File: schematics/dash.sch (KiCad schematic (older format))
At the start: 28 parts, among them J1 BATT_CONN, J2 EXTERNAL_TRIGGER, J3 USB_OTG, SW1 SW_Push, SW2 SW_Push, U1 ESP-12E, U2 ch340g, U3 MCP73833, U4 HT7333, Y1 12Mhz

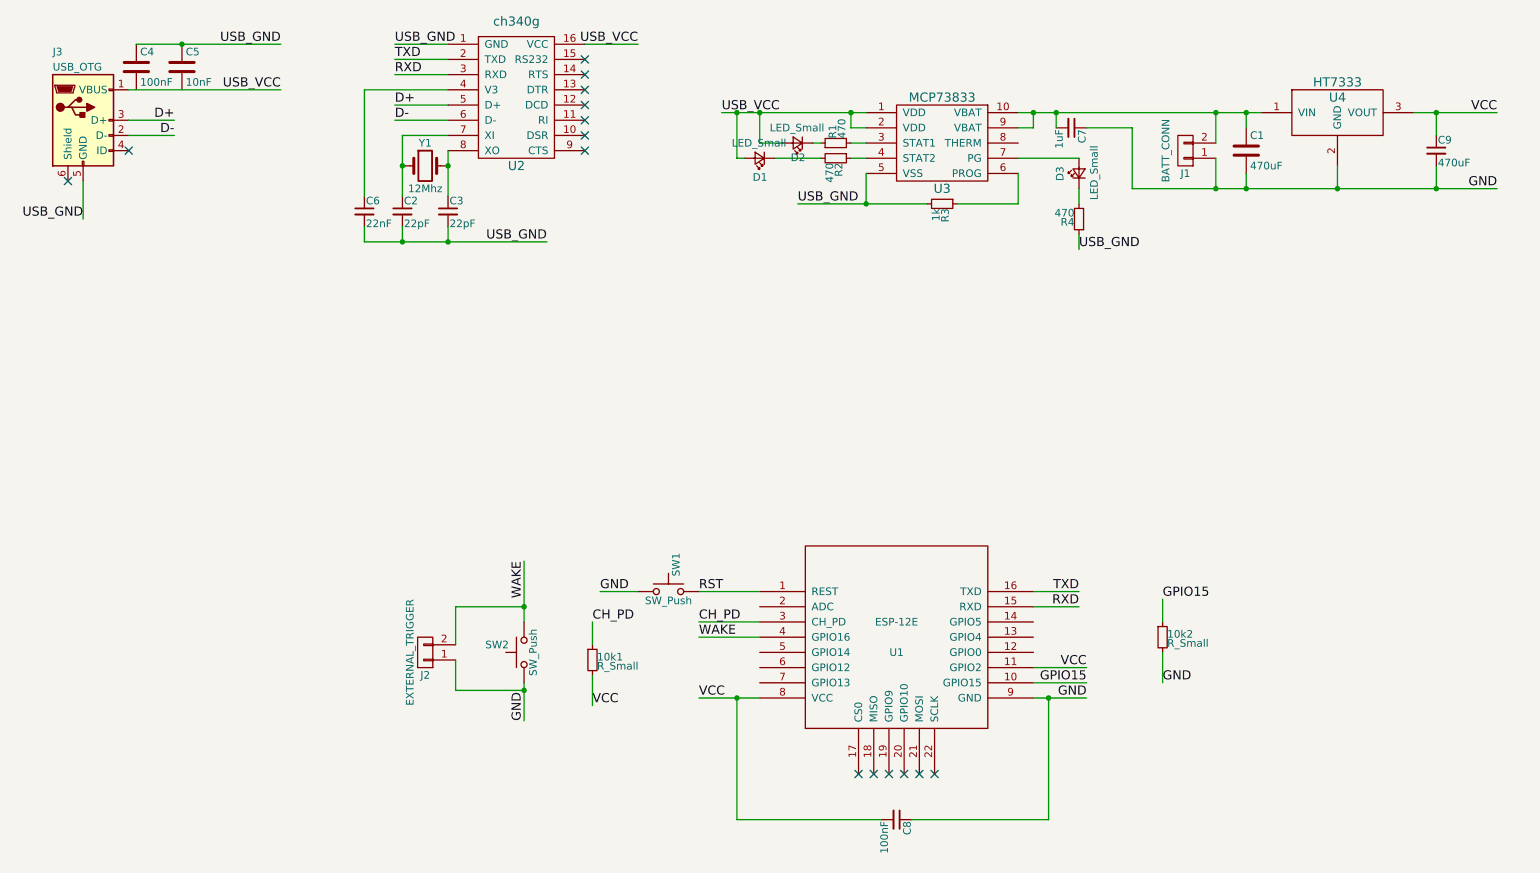
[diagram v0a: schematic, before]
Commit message: [add] Correction on boot mode pins
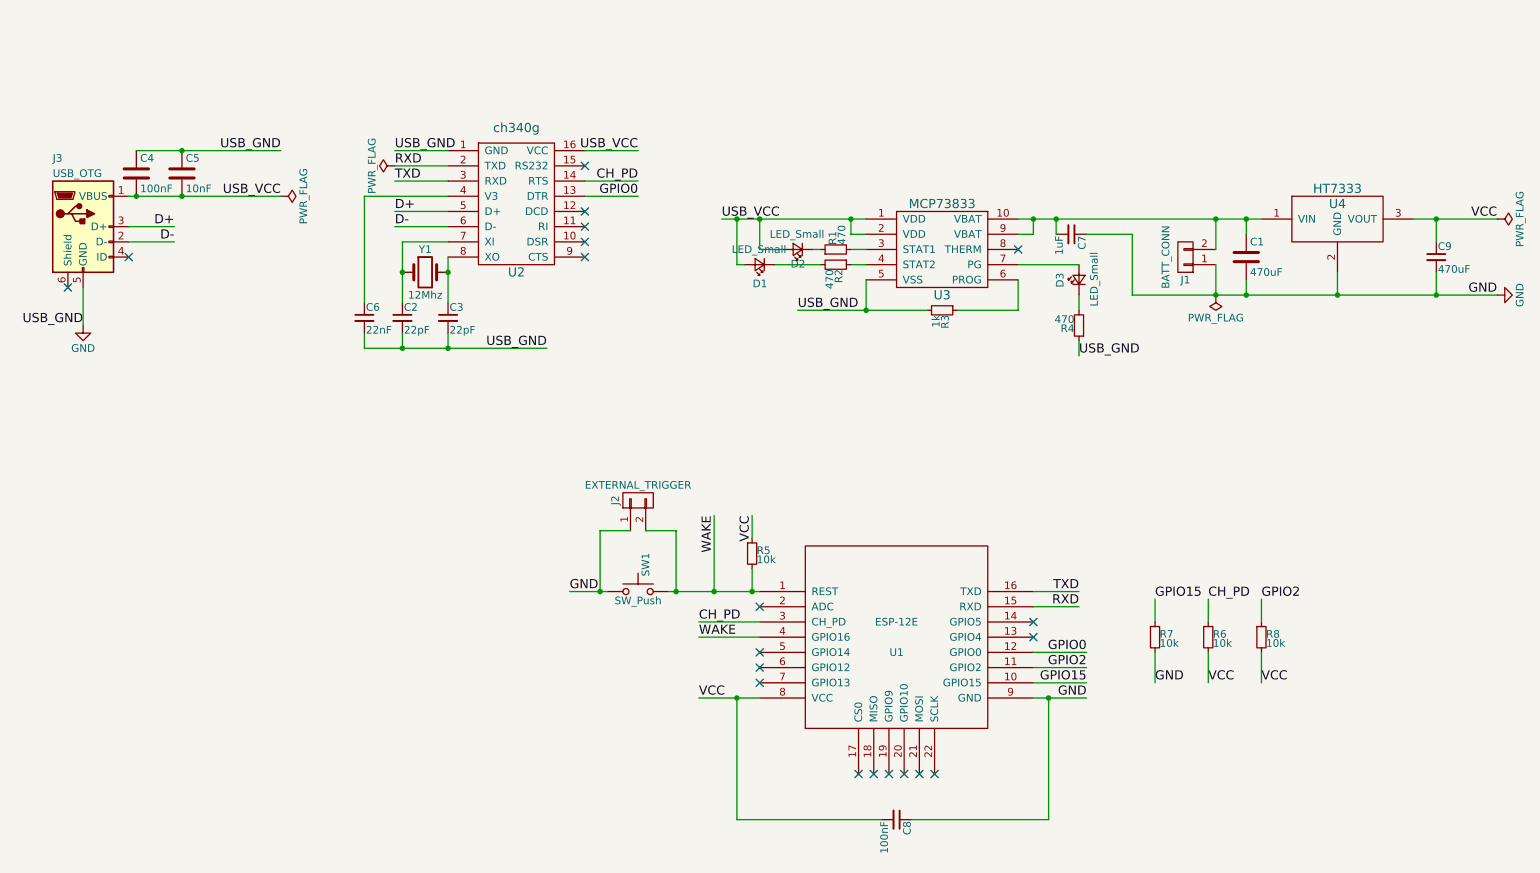
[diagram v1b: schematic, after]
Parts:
- removed 10k1, 10k2: R_Small, symbol R_Small
- removed SW2: SW_Push, symbol SW_Push
- added R5, R6, R7, R8: 10k, symbol R_Small
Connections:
- net RST is gone; now on net WAKE: SW1.2, U1.1 (REST)
- net USB_GND is gone; now on net GND: C2.2, C3.2, C4.1, C5.1, C6.2, J3.5 (GND), R3.2, R4.1, U2.1 (GND), U3.5 (VSS)
- net CH_PD: now also U2.14 (RTS), R6.1
- net GND: now also R7.2
- net GPIO15: now also R7.1
- net RXD: now also U2.2 (TXD); no longer U2.3 (RXD)
- net TXD: now also U2.3 (RXD); no longer U2.2 (TXD)
- net USB_VCC: now also C4.2, C5.2
- net VCC: now also R5.1, R6.2, R8.2; no longer U1.11 (GPIO2)
- net WAKE: now also R5.2
- net GPIO0: now reaches U1.12 (GPIO0)
- net GPIO0: now also U2.13 (DTR)
- new net GPIO2: R8.1, U1.11 (GPIO2)
- no-connect marks 15 -> 20
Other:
- moved on the sheet: C1, C2, C3, C4, C5, C6, C7, C9, D1, D2, D3, J1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

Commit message: add libraries to project and link symbols with footprints
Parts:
- C1, C2, C3, C4, C5, C6, C8: footprint (none) -> Capacitors_SMD:C_1206_HandSoldering
- C7: footprint (none) -> Capacitors_Tantalum_SMD:Tantalum_Case-A_EIA-3216-18_Hand
- C9: footprint (none) -> Capacitors_Tantalum_SMD:Tantalum_Case-D_EIA-7343-31_Hand
- D1, D2, D3: footprint (none) -> LEDs:LED_1206
- J1: footprint (none) -> Pin_Headers:Pin_Header_Angled_1x02
- J2: footprint (none) -> Pin_Headers:Pin_Header_Straight_1x02
- J3: footprint (none) -> Connect:USB_Micro-B; symbol USB_OTG -> USB_OTG-RESCUE-dash
- R1, R2, R3, R4, R5, R6, R7, R8: footprint (none) -> Resistors_SMD:R_1206_HandSoldering
- SW1: footprint (none) -> Buttons_Switches_ThroughHole:SW_PUSH_6mm
- U1: footprint (none) -> ESP8266:ESP-12E_SMD
- U2: footprint (none) -> SMD_Packages:SO-16-N
- U3: footprint (none) -> sop:MSOP10
- U4: footprint (none) -> TO_SOT_Packages_SMD:SOT89-3_Housing_Handsoldering
- Y1: footprint (none) -> Crystals:Crystal_HC49-U_Vertical
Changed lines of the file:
@@
 EESchema Schematic File Version 2
+LIBS:dash-rescue
 LIBS:power
 LIBS:device
@@
 LIBS:contrib
 LIBS:valves
-LIBS:ESP8266
 LIBS:switches
 LIBS:ch340g
+LIBS:ESP8266
 LIBS:dash-cache
 EELAYER 25 0
@@
 F 0 "U1" H 6650 4550 50  0000 C CNN
 F 1 "ESP-12E" H 6650 4750 50  0000 C CNN
-F 2 "" H 6650 4650 50  0001 C CNN
+F 2 "ESP8266:ESP-12E_SMD" H 6650 4650 50  0001 C CNN
 F 3 "" H 6650 4650 50  0001 C CNN
 	1    6650 4650
@@
 F 0 "SW1" V 5000 4450 50  0000 L CNN
 F 1 "SW_Push" H 4950 4290 50  0000 C CNN
-F 2 "" H 4950 4550 50  0001 C CNN
+F 2 "Buttons_Switches_ThroughHole:SW_PUSH_6mm" H 4950 4550 50  0001 C CNN
 F 3 "" H 4950 4550 50  0001 C CNN
 	1    4950 4350
@@
 F 0 "C1" H 8975 2250 50  0000 L CNN
 F 1 "470uF" H 8975 2050 50  0000 L CNN
-F 2 "" H 8988 2000 50  0001 C CNN
+F 2 "Capacitors_SMD:C_1206_HandSoldering" H 8988 2000 50  0001 C CNN
 F 3 "" H 8950 2150 50  0001 C CNN
 	1    8950 2150
@@
 F 0 "J1" H 8550 2300 50  0000 C CNN
 F 1 "BATT_CONN" V 8650 2150 50  0000 C TNN
-F 2 "" H 8550 2150 50  0001 C CNN
+F 2 "Pin_Headers:Pin_Header_Angled_1x02" H 8550 2150 50  0001 C CNN
 F 3 "" H 8550 2150 50  0001 C CNN
 	1    8550 2150
@@
 F 0 "J2" H 4950 3900 50  0000 C CNN
 F 1 "EXTERNAL_TRIGGER" V 5050 3750 50  0000 C CNN
-F 2 "" H 4950 3750 50  0001 C CNN
+F 2 "Pin_Headers:Pin_Header_Straight_1x02" H 4950 3750 50  0001 C CNN
 F 3 "" H 4950 3750 50  0001 C CNN
 	1    4950 3750
@@
 $EndComp
 $Comp
-L USB_OTG J3
+L USB_OTG-RESCUE-dash J3
 U 1 1 59611B73
 P 1300 1950
 F 0 "J3" H 1100 2400 50  0000 L CNN
 F 1 "USB_OTG" H 1100 2300 50  0000 L CNN
-F 2 "" H 1450 1900 50  0001 C CNN
+F 2 "Connect:USB_Micro-B" H 1450 1900 50  0001 C CNN
 F 3 "" H 1450 1900 50  0001 C CNN
 	1    1300 1950
@@
 F 0 "U2" H 4150 1050 60  0000 C CNN
 F 1 "ch340g" H 4150 2000 60  0000 C CNN
-F 2 "" H 3950 1650 60  0001 C CNN
+F 2 "SMD_Packages:SO-16-N" H 3950 1650 60  0001 C CNN
 F 3 "" H 3950 1650 60  0001 C CNN
 	1    4150 1650
@@
 F 0 "Y1" H 3550 2400 50  0000 C CNN
 F 1 "12Mhz" H 3550 2100 50  0000 C CNN
-F 2 "" H 3550 2250 50  0001 C CNN
+F 2 "Crystals:Crystal_HC49-U_Vertical" H 3550 2250 50  0001 C CNN
 F 3 "" H 3550 2250 50  0001 C CNN
 	1    3550 2250
@@
 F 0 "C2" H 3410 2620 50  0000 L CNN
 F 1 "22pF" H 3410 2470 50  0000 L CNN
-F 2 "" H 3400 2550 50  0001 C CNN
+F 2 "Capacitors_SMD:C_1206_HandSoldering" H 3400 2550 50  0001 C CNN
 F 3 "" H 3400 2550 50  0001 C CNN
 	1    3400 2550
@@
 F 0 "C3" H 3710 2620 50  0000 L CNN
 F 1 "22pF" H 3710 2470 50  0000 L CNN
-F 2 "" H 3700 2550 50  0001 C CNN
+F 2 "Capacitors_SMD:C_1206_HandSoldering" H 3700 2550 50  0001 C CNN
 F 3 "" H 3700 2550 50  0001 C CNN
 	1    3700 2550
@@
 F 0 "C4" H 1675 1700 50  0000 L CNN
 F 1 "100nF" H 1675 1500 50  0000 L CNN
-F 2 "" H 1688 1450 50  0001 C CNN
+F 2 "Capacitors_SMD:C_1206_HandSoldering" H 1688 1450 50  0001 C CNN
 F 3 "" H 1650 1600 50  0001 C CNN
 	1    1650 1600
@@
 F 0 "C5" H 1975 1700 50  0000 L CNN
 F 1 "10nF" H 1975 1500 50  0000 L CNN
-F 2 "" H 1988 1450 50  0001 C CNN
+F 2 "Capacitors_SMD:C_1206_HandSoldering" H 1988 1450 50  0001 C CNN
 F 3 "" H 1950 1600 50  0001 C CNN
 	1    1950 1600
@@
 F 0 "C6" H 3160 2620 50  0000 L CNN
 F 1 "22nF" H 3160 2470 50  0000 L CNN
-F 2 "" H 3150 2550 50  0001 C CNN
+F 2 "Capacitors_SMD:C_1206_HandSoldering" H 3150 2550 50  0001 C CNN
 F 3 "" H 3150 2550 50  0001 C CNN
 	1    3150 2550
@@
 F 0 "U3" H 6950 1900 60  0000 C CNN
 F 1 "MCP73833" H 6950 2500 60  0000 C CNN
-F 2 "" H 6950 2150 60  0001 C CNN
+F 2 "sop:MSOP10" H 6950 2150 60  0001 C CNN
 F 3 "" H 6950 2150 60  0001 C CNN
 	1    6950 2150
@@
 F 0 "D2" H 5950 2225 50  0000 L TNN
 F 1 "LED_Small" H 5825 2000 50  0000 L CNN
-F 2 "" V 6000 2100 50  0001 C CNN
+F 2 "LEDs:LED_1206" V 6000 2100 50  0001 C CNN
 F 3 "" V 6000 2100 50  0001 C CNN
 	1    6000 2100
@@
 F 0 "R1" H 6280 2120 50  0000 L CNN
 F 1 "470" H 6280 2060 50  0000 L CNN
-F 2 "" H 6250 2100 50  0001 C CNN
+F 2 "Resistors_SMD:R_1206_HandSoldering" H 6250 2100 50  0001 C CNN
 F 3 "" H 6250 2100 50  0001 C CNN
 	1    6250 2100
@@
 F 0 "R2" H 6280 2220 50  0000 L CNN
 F 1 "470" H 6280 2160 50  0000 L CNN
-F 2 "" H 6250 2200 50  0001 C CNN
+F 2 "Resistors_SMD:R_1206_HandSoldering" H 6250 2200 50  0001 C CNN
 F 3 "" H 6250 2200 50  0001 C CNN
 	1    6250 2200
@@
 F 0 "D1" H 5700 2325 50  0000 L CNN
 F 1 "LED_Small" H 5575 2100 50  0000 L CNN
-F 2 "" V 5750 2200 50  0001 C CNN
+F 2 "LEDs:LED_1206" V 5750 2200 50  0001 C CNN
 F 3 "" V 5750 2200 50  0001 C CNN
 	1    5750 2200
@@
 F 0 "R3" H 6980 2520 50  0000 L CNN
 F 1 "1k" H 6980 2460 50  0000 L CNN
-F 2 "" H 6950 2500 50  0001 C CNN
+F 2 "Resistors_SMD:R_1206_HandSoldering" H 6950 2500 50  0001 C CNN
 F 3 "" H 6950 2500 50  0001 C CNN
 	1    6950 2500
@@
 F 0 "C7" H 7810 2070 50  0000 L CNN
 F 1 "1uF" H 7810 1920 50  0000 L CNN
-F 2 "" H 7800 2000 50  0001 C CNN
+F 2 "Capacitors_Tantalum_SMD:Tantalum_Case-A_EIA-3216-18_Hand" H 7800 2000 50  0001 C CNN
 F 3 "" H 7800 2000 50  0001 C CNN
 	1    7800 2000
@@
 F 0 "D3" H 7800 2425 50  0000 L CNN
 F 1 "LED_Small" H 7675 2200 50  0000 L CNN
-F 2 "" V 7850 2300 50  0001 C CNN
+F 2 "LEDs:LED_1206" V 7850 2300 50  0001 C CNN
 F 3 "" V 7850 2300 50  0001 C CNN
 	1    7850 2300
@@
 F 0 "R4" H 7880 2620 50  0000 L CNN
 F 1 "470" H 7880 2560 50  0000 L CNN
-F 2 "" H 7850 2600 50  0001 C CNN
+F 2 "Resistors_SMD:R_1206_HandSoldering" H 7850 2600 50  0001 C CNN
 F 3 "" H 7850 2600 50  0001 C CNN
 	1    7850 2600
@@
 F 0 "C8" H 6660 5920 50  0000 L CNN
 F 1 "100nF" H 6660 5770 50  0000 L CNN
-F 2 "" H 6650 5850 50  0001 C CNN
+F 2 "Capacitors_SMD:C_1206_HandSoldering" H 6650 5850 50  0001 C CNN
 F 3 "" H 6650 5850 50  0001 C CNN
 	1    6650 5850
@@
 F 0 "C9" H 10210 2220 50  0000 L CNN
 F 1 "470uF" H 10210 2070 50  0000 L CNN
-F 2 "" H 10200 2150 50  0001 C CNN
+F 2 "Capacitors_Tantalum_SMD:Tantalum_Case-D_EIA-7343-31_Hand" H 10200 2150 50  0001 C CNN
 F 3 "" H 10200 2150 50  0001 C CNN
 	1    10200 2150
@@
 F 0 "U4" H 9550 2000 60  0000 C CNN
 F 1 "HT7333" H 9550 2100 60  0000 C CNN
-F 2 "" H 9550 1900 60  0001 C CNN
+F 2 "TO_SOT_Packages_SMD:SOT89-3_Housing_Handsoldering" H 9550 1900 60  0001 C CNN
 F 3 "" H 9550 1900 60  0001 C CNN
 	1    9550 1900
@@
 F 0 "R5" H 5730 4120 50  0000 L CNN
 F 1 "10k" H 5730 4060 50  0000 L CNN
-F 2 "" H 5700 4100 50  0001 C CNN
+F 2 "Resistors_SMD:R_1206_HandSoldering" H 5700 4100 50  0001 C CNN
 F 3 "" H 5700 4100 50  0001 C CNN
 	1    5700 4100
@@
 F 0 "R6" H 8730 4670 50  0000 L CNN
 F 1 "10k" H 8730 4610 50  0000 L CNN
-F 2 "" H 8700 4650 50  0001 C CNN
+F 2 "Resistors_SMD:R_1206_HandSoldering" H 8700 4650 50  0001 C CNN
 F 3 "" H 8700 4650 50  0001 C CNN
 	1    8700 4650
@@
 F 0 "R7" H 8380 4670 50  0000 L CNN
 F 1 "10k" H 8380 4610 50  0000 L CNN
-F 2 "" H 8350 4650 50  0001 C CNN
+F 2 "Resistors_SMD:R_1206_HandSoldering" H 8350 4650 50  0001 C CNN
 F 3 "" H 8350 4650 50  0001 C CNN
 	1    8350 4650
@@
 F 0 "R8" H 9080 4670 50  0000 L CNN
 F 1 "10k" H 9080 4610 50  0000 L CNN
-F 2 "" H 9050 4650 50  0001 C CNN
+F 2 "Resistors_SMD:R_1206_HandSoldering" H 9050 4650 50  0001 C CNN
 F 3 "" H 9050 4650 50  0001 C CNN
 	1    9050 4650

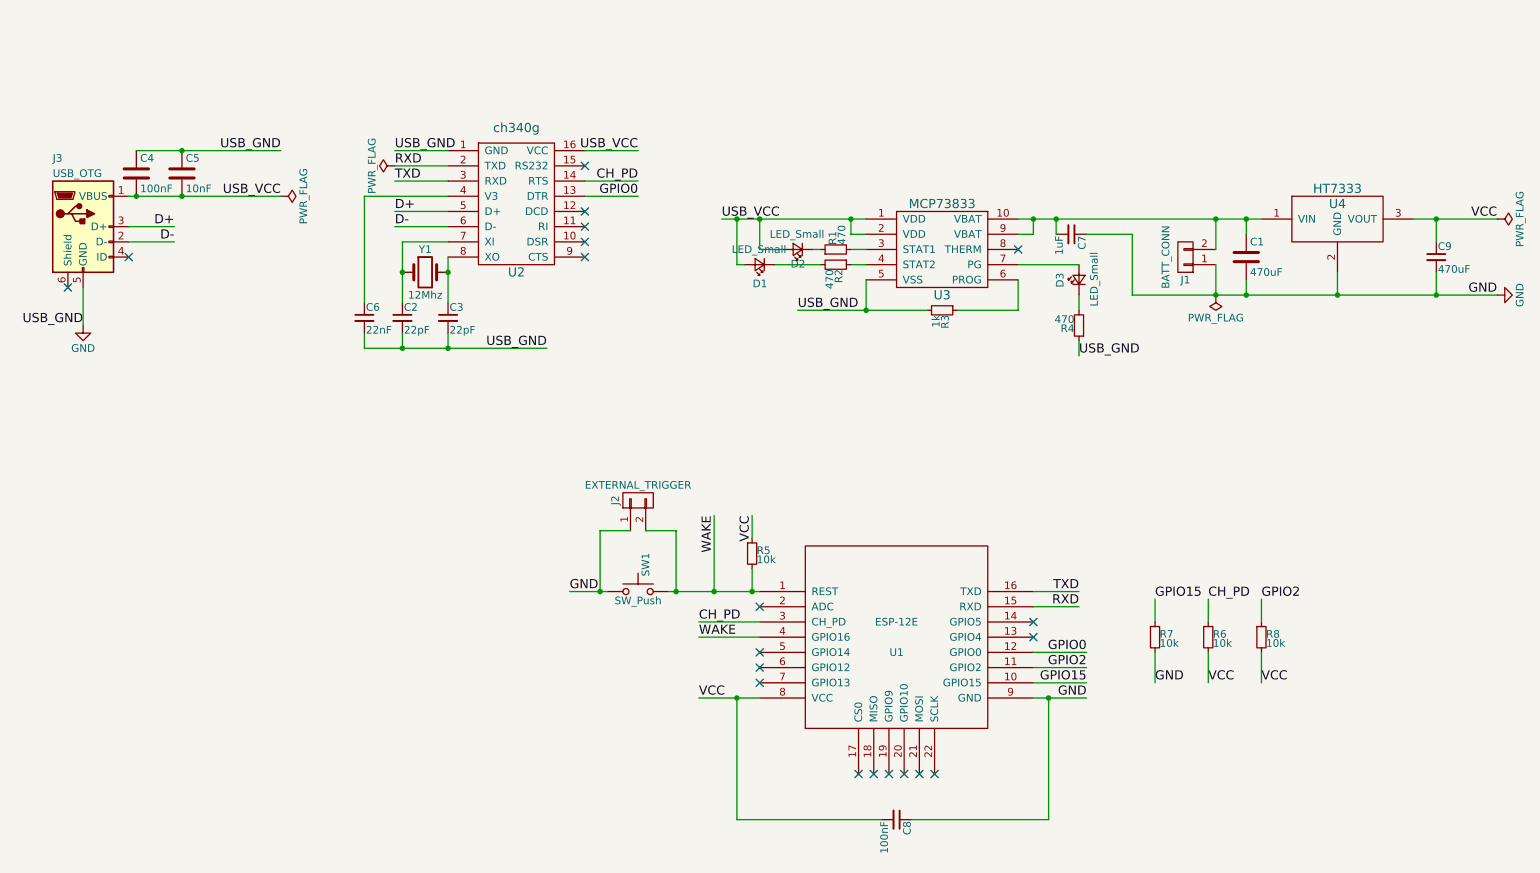
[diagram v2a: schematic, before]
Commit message: [enh] Better power port placement with fixed pin mode for ICs
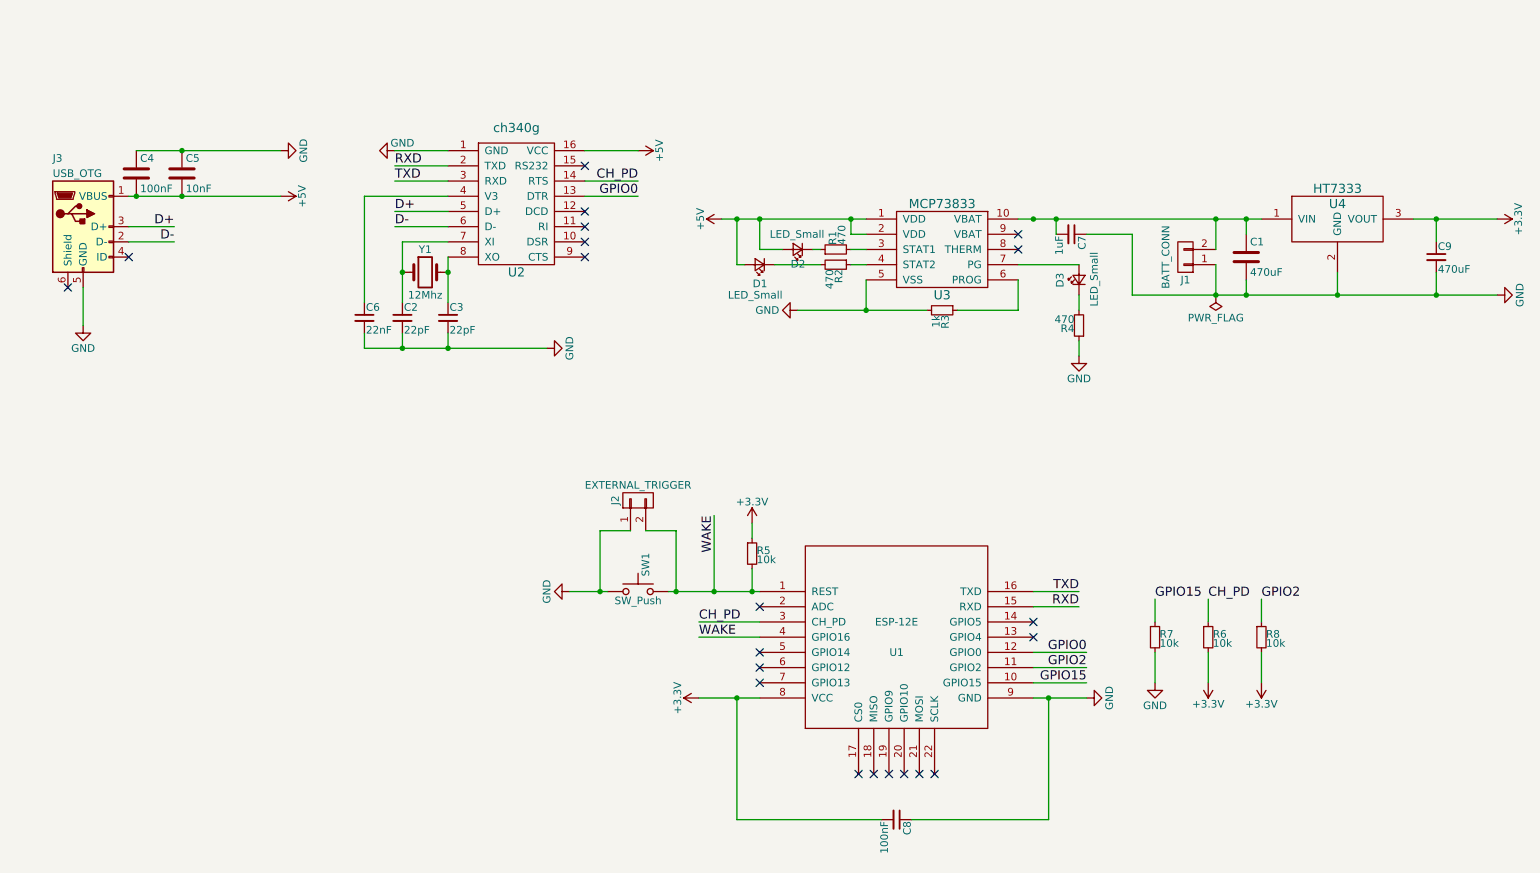
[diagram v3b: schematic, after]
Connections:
- net at C1.1, C7.2, J1.2 (P2)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: no longer U3.9 (VBAT)
- net USB_VCC renamed +5V
- net VCC renamed +3V3
- no-connect marks 20 -> 21
